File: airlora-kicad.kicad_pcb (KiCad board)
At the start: 4 copper layers, 77 x 77 mm, 125 parts, among them IC1 BALFHB-WL-02D3, J1 12V, J10 I2C, J11 UART2, J2 Conn_Coaxial, J3 Led, J4 SHT, J5 I2C, J6 A_NO2, J7 UART1, J8 A_CO, J9 I2C, Q10 S8050, Q2 S8050, Q3 S8050, Q4 S8050, Q5 S8050, Q6 S8050, Q7 S8050, Q8 S8050, Q9 S8050, SW1 SW_Push, SW2 SW_Slide_DPDT, SW3 SW_Push, U1 TPS7A2633DRVR, U2 TPS54202DDC, U3 TPS7A2633DRVR, U4 BGS12WN6E6327, U6 STM32F103C8Tx, U7 STM32WLE5CCUx, X1 32MHZ, Y1 32.768kHz, Y2 8Mhz

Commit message: Update PCB layout
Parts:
- added G***: LOGO, footprint:CAMBODIA 10mm, F.Cu at (90.9, 101.4)
- added G***: LOGO, footprint:Chiptree_logo 6mm, F.Cu at (99.6, 101.5)
- added kibuzzard-667528BC: G***, kibuzzard-667528BC, F.Cu at (115.4, 99.5)
- added kibuzzard-667528D4: G***, kibuzzard-667528D4, F.Cu at (110.4, 99.6)
- added kibuzzard-66752922: G***, kibuzzard-66752922, F.Cu at (83.9, 123.3)
- added kibuzzard-66752922: G***, kibuzzard-66752922, B.Cu at (104.2, 55.6)
- added kibuzzard-66752922: G***, kibuzzard-66752922, F.Cu at (71.0, 123.3)
- added kibuzzard-66752922: G***, kibuzzard-66752922, F.Cu at (121.4, 96.5)
- added kibuzzard-66752922: G***, kibuzzard-66752922, B.Cu at (124.1, 87.6)
- added kibuzzard-66752922: G***, kibuzzard-66752922, B.Cu at (91.6, 55.6)
- added kibuzzard-66752922: G***, kibuzzard-66752922, B.Cu at (116.8, 55.6)
- added kibuzzard-66752922: G***, kibuzzard-66752922, B.Cu at (123.9, 76.0)
- added kibuzzard-66752922: G***, kibuzzard-66752922, B.Cu at (78.8, 55.7)
- added kibuzzard-66752922: G***, kibuzzard-66752922, B.Cu at (123.6, 61.7)
- added kibuzzard-66752939: G***, kibuzzard-66752939, F.Cu at (121.4, 99.0)
- added kibuzzard-66752971: G***, kibuzzard-66752971, F.Cu at (121.4, 104.0)
- added kibuzzard-66752981: G***, kibuzzard-66752981, F.Cu at (121.4, 101.5)
- added kibuzzard-66753395: G***, kibuzzard-66753395, F.Cu at (76.1, 123.3)
- added kibuzzard-667540EB: G***, kibuzzard-667540EB, B.Cu at (105.9, 55.6)
- added kibuzzard-667540EB: G***, kibuzzard-667540EB, B.Cu at (93.3, 55.6)
- added kibuzzard-667540EB: G***, kibuzzard-667540EB, B.Cu at (123.6, 59.2)
- added kibuzzard-667540EB: G***, kibuzzard-667540EB, B.Cu at (118.5, 55.6)
- added kibuzzard-667540EB: G***, kibuzzard-667540EB, B.Cu at (124.1, 85.1)
- added kibuzzard-667540EB: G***, kibuzzard-667540EB, B.Cu at (80.4, 55.7)
- added kibuzzard-667540EB: G***, kibuzzard-667540EB, B.Cu at (123.9, 73.6)
- added kibuzzard-66754104: G***, kibuzzard-66754104, B.Cu at (123.9, 78.4)
- added kibuzzard-66754176: G***, kibuzzard-66754176, F.Cu at (96.7, 89.6)
- added kibuzzard-66754176: G***, kibuzzard-66754176, F.Cu at (125.2, 116.2)
- added kibuzzard-667541A7: G***, kibuzzard-667541A7, F.Cu at (88.8, 123.3)
- added kibuzzard-667541BE: G***, kibuzzard-667541BE, B.Cu at (77.1, 55.7)
- added kibuzzard-667541C9: G***, kibuzzard-667541C9, B.Cu at (75.4, 55.7)
- added kibuzzard-667541E6: G***, kibuzzard-667541E6, B.Cu at (100.9, 55.3)
- added kibuzzard-667541E6: G***, kibuzzard-667541E6, B.Cu at (123.6, 66.7)
- added kibuzzard-667541E6: G***, kibuzzard-667541E6, B.Cu at (88.3, 55.3)
- added kibuzzard-667541E6: G***, kibuzzard-667541E6, B.Cu at (113.5, 55.3)
- added kibuzzard-667541EF: G***, kibuzzard-667541EF, B.Cu at (102.5, 55.3)
- added kibuzzard-667541EF: G***, kibuzzard-667541EF, B.Cu at (89.9, 55.3)
- added kibuzzard-667541EF: G***, kibuzzard-667541EF, B.Cu at (123.6, 64.2)
- added kibuzzard-667541EF: G***, kibuzzard-667541EF, B.Cu at (115.1, 55.3)
- added kibuzzard-66754524: G***, kibuzzard-66754524, B.Cu at (124.1, 90.1)
- added kibuzzard-66763AB2: G***, kibuzzard-66763AB2, F.Cu at (81.0, 82.2)
- added kibuzzard-66763ACD: G***, kibuzzard-66763ACD, F.Cu at (81.7, 87.9)
- added kibuzzard-66763ACD: G***, kibuzzard-66763ACD, F.Cu at (81.8, 76.0)
- moved R27 0.79 mm to (93.8, 67.0)
- moved Q10 0.78 mm to (93.0, 64.5)
- moved Q9 0.68 mm to (105.8, 64.5)
- moved R26 0.66 mm to (106.5, 67.0)
- moved J3 0.39 mm to (88.9, 118.1)
- moved Q4 0.34 mm to (118.5, 64.6)
- moved R21 0.33 mm to (119.2, 67.0)
- moved C8 0.33 mm to (71.9, 94.5)
- moved C7 0.17 mm to (74.2, 94.5)
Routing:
- net +5V: track 191.1 -> 186.8 mm
- net +3.3V: track 104.0 -> 106.0 mm, vias 9 -> 8
- net +3.3V_HP: track 73.2 -> 74.7 mm, vias 12 -> 9
- net Net-(U6-NRST): track 19.0 -> 20.1 mm
- net /AirLora V3/MCU Sub/PB3: track 13.4 -> 12.4 mm
- net /AirLora V3/MCU/PA6: track 33.0 -> 34.0 mm
- net /AirLora V3/MCU Sub/PB4: track 16.0 -> 16.9 mm
- net /AirLora V3/MCU Sub/PA4: track 23.9 -> 24.6 mm
- net Net-(J10-Pin_2): track 5.06 -> 4.46 mm
- net GND: vias 96 -> 213

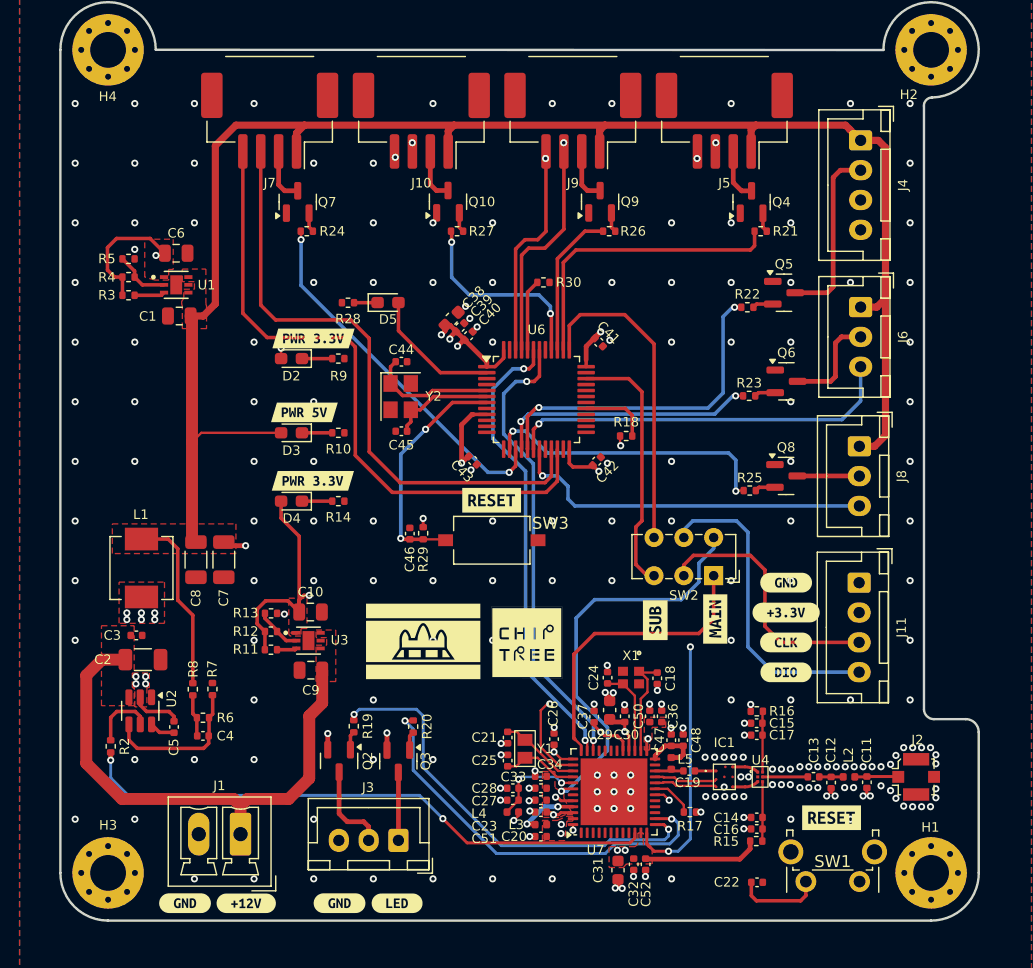
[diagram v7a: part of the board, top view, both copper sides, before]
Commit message: Update PCB layout and add Logo
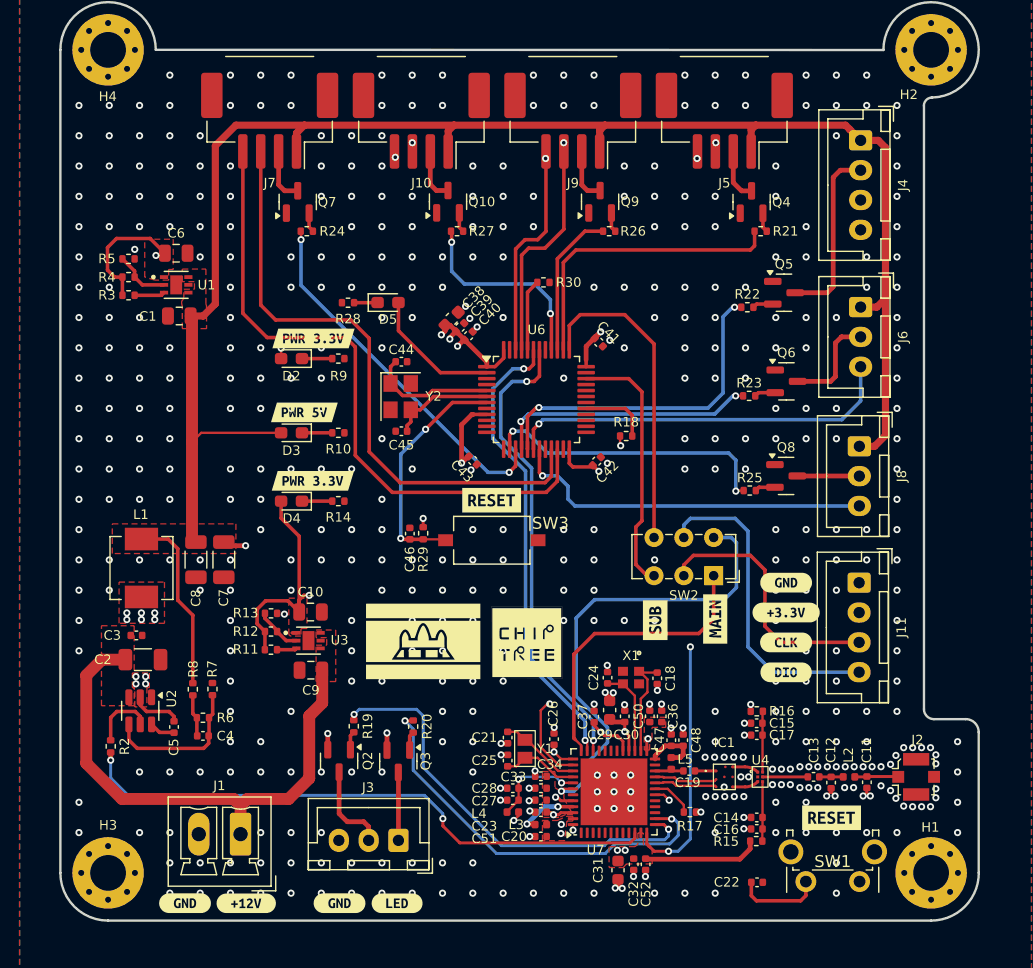
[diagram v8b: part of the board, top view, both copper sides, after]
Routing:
- net /AirLora V3/MCU/T_SWCLK: track 34.3 -> 39.2 mm
- net /AirLora V3/MCU/PA3: track 49.0 -> 49.5 mm
- net GND: vias 213 -> 484
